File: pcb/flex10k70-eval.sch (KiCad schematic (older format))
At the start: 68 parts, among them CN1 IO_1, CN2 IO_2, CN3 IO_3, CN4 IO_4, CN5 FLASH, CN6 JTAG, SW1 SW_DIP_x04, SW2 SW_DIP_x04, U1 25LC1024-I/SM, U2 EPF10K70RC240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

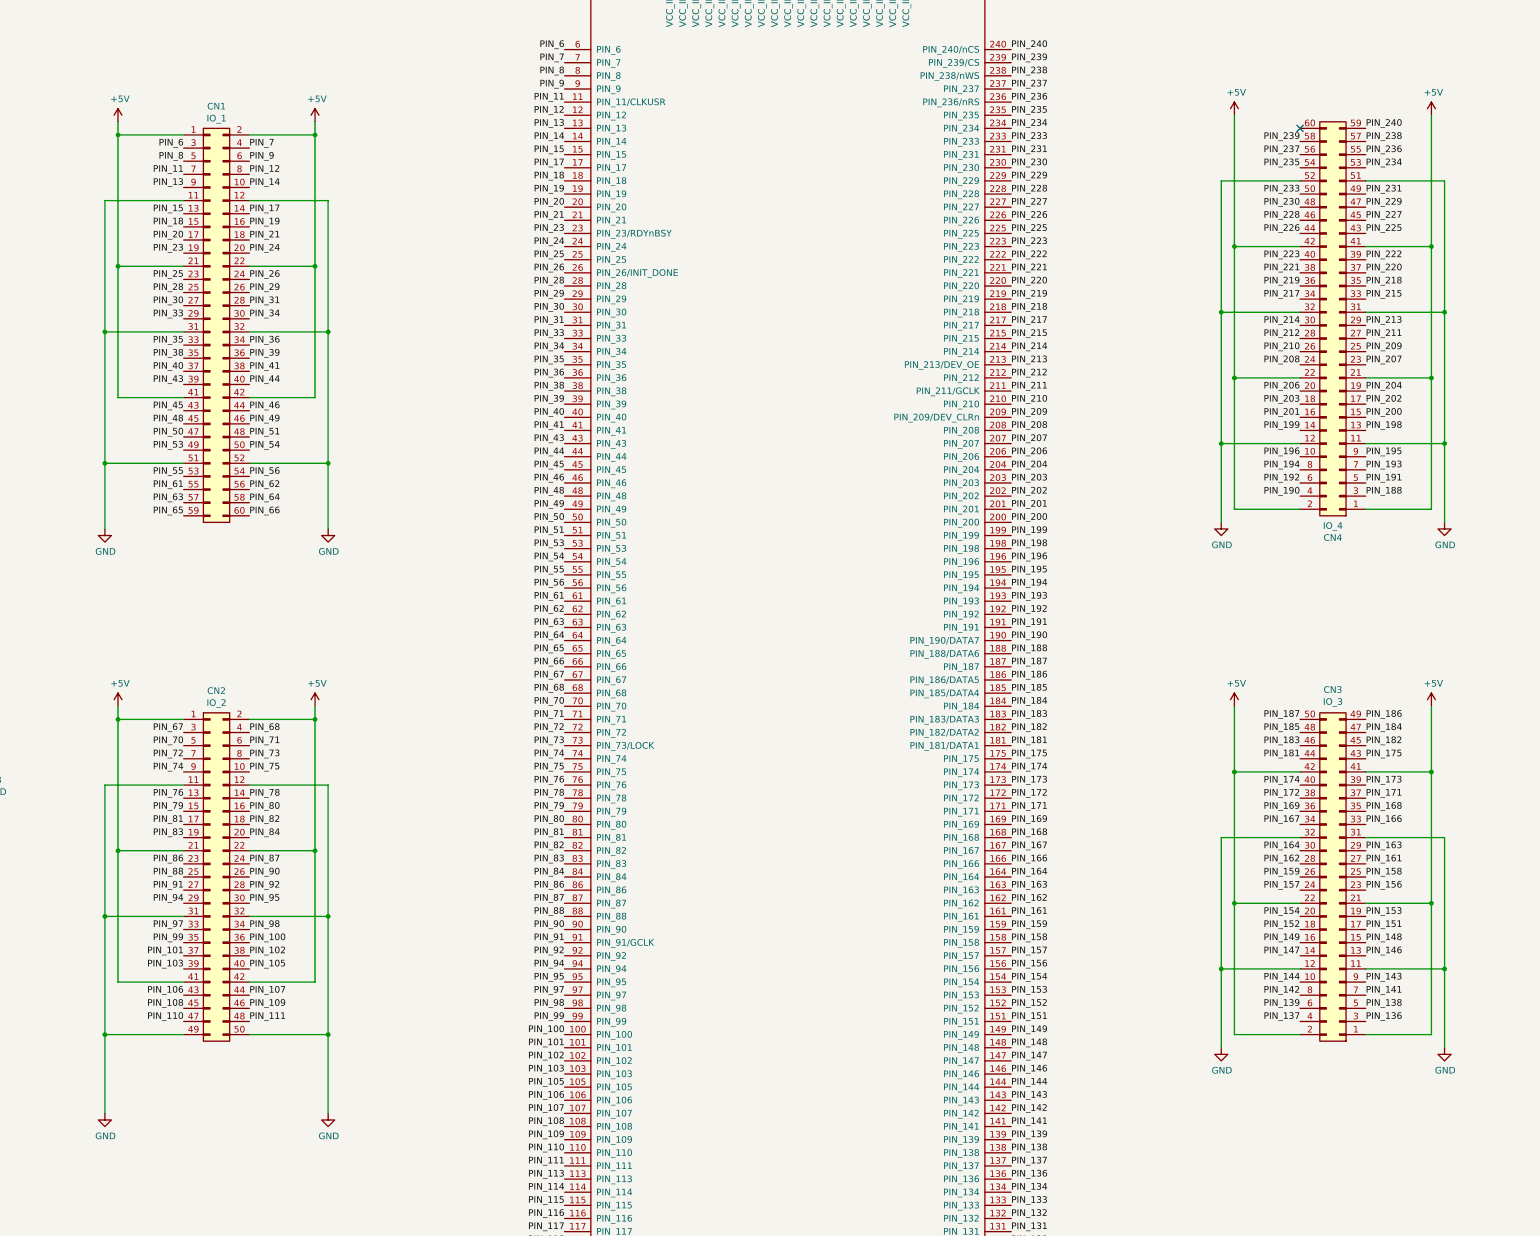
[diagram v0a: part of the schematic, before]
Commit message: modify CN3 CN4 pin orientation
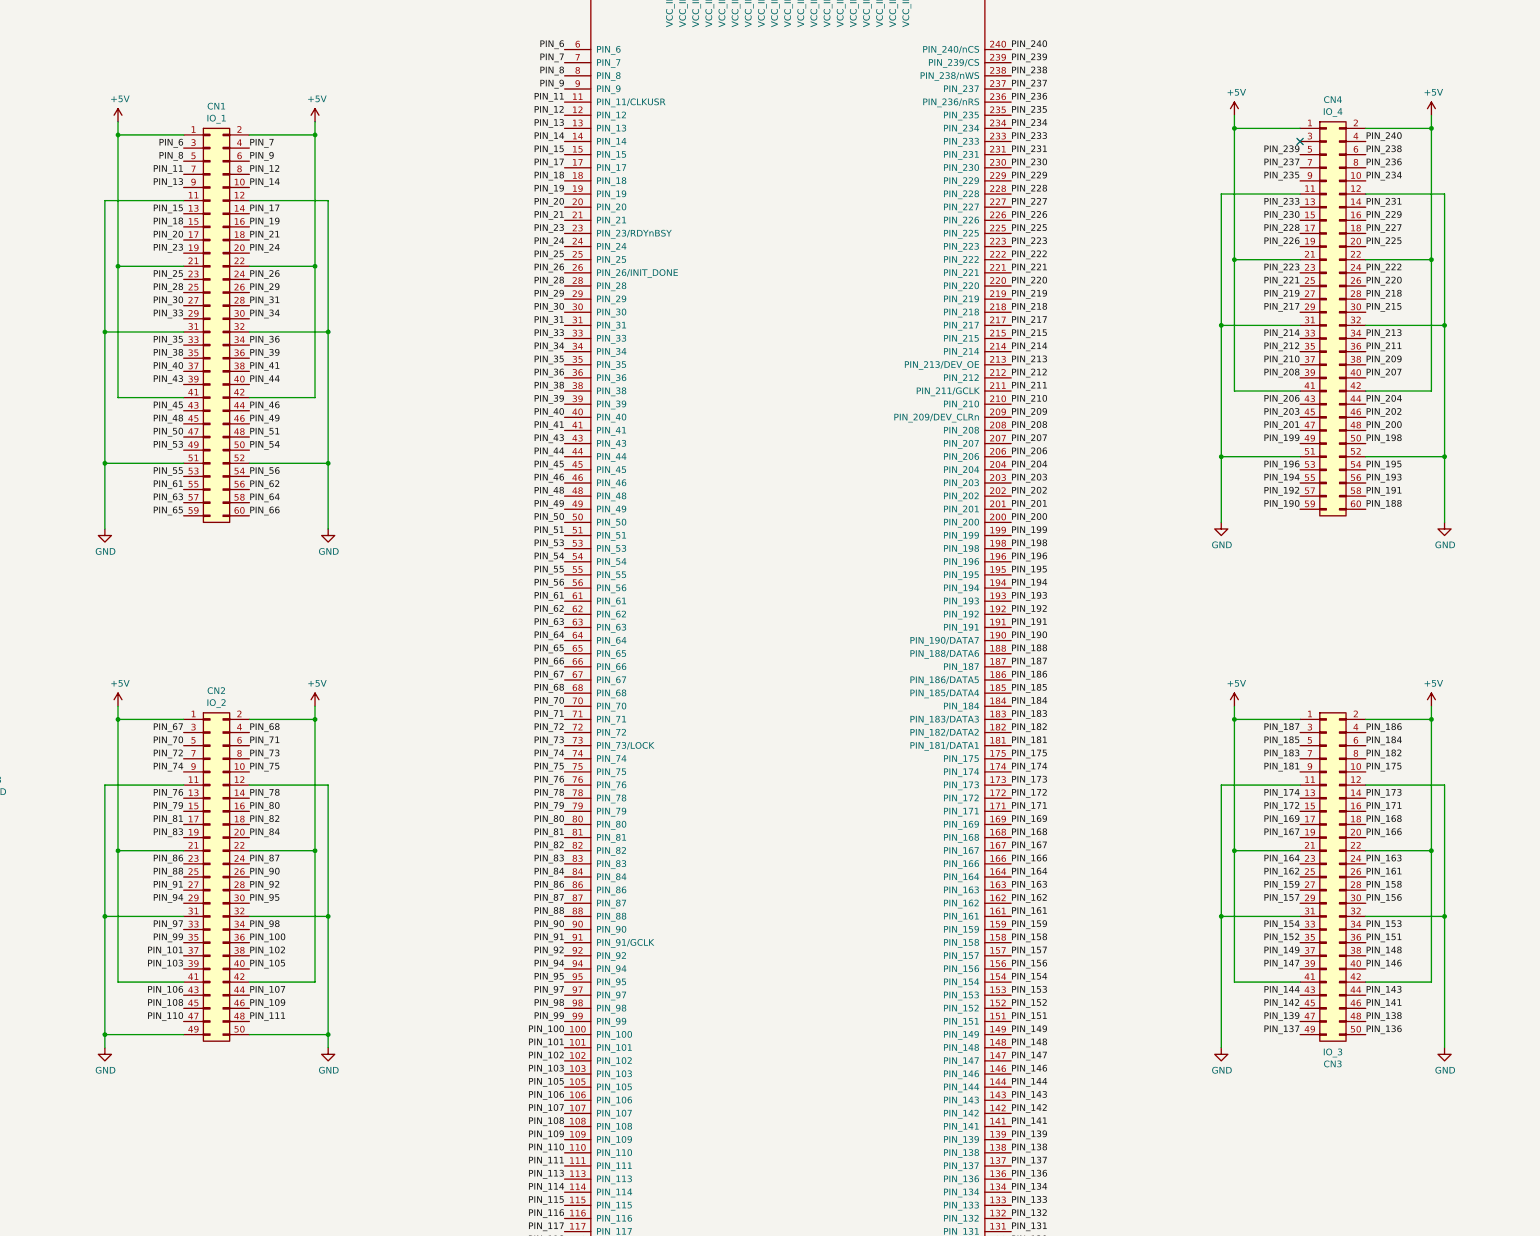
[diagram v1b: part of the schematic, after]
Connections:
- net PIN_136: now also CN3.50 (Pin_50); no longer CN3.3 (Pin_3)
- net PIN_137: now also CN3.49 (Pin_49); no longer CN3.4 (Pin_4)
- net PIN_138: now also CN3.48 (Pin_48); no longer CN3.5 (Pin_5)
- net PIN_139: now also CN3.47 (Pin_47); no longer CN3.6 (Pin_6)
- net PIN_141: now also CN3.46 (Pin_46); no longer CN3.7 (Pin_7)
- net PIN_142: now also CN3.45 (Pin_45); no longer CN3.8 (Pin_8)
- net PIN_143: now also CN3.44 (Pin_44); no longer CN3.9 (Pin_9)
- net PIN_144: now also CN3.43 (Pin_43); no longer CN3.10 (Pin_10)
- net PIN_146: now also CN3.40 (Pin_40); no longer CN3.13 (Pin_13)
- net PIN_147: now also CN3.39 (Pin_39); no longer CN3.14 (Pin_14)
- net PIN_148: now also CN3.38 (Pin_38); no longer CN3.15 (Pin_15)
- net PIN_149: now also CN3.37 (Pin_37); no longer CN3.16 (Pin_16)
- net PIN_151: now also CN3.36 (Pin_36); no longer CN3.17 (Pin_17)
- net PIN_152: now also CN3.35 (Pin_35); no longer CN3.18 (Pin_18)
- net PIN_153: now also CN3.34 (Pin_34); no longer CN3.19 (Pin_19)
- net PIN_154: now also CN3.33 (Pin_33); no longer CN3.20 (Pin_20)
- net PIN_156: now also CN3.30 (Pin_30); no longer CN3.23 (Pin_23)
- net PIN_157: now also CN3.29 (Pin_29); no longer CN3.24 (Pin_24)
- net PIN_158: now also CN3.28 (Pin_28); no longer CN3.25 (Pin_25)
- net PIN_159: now also CN3.27 (Pin_27); no longer CN3.26 (Pin_26)
- net PIN_161: now also CN3.26 (Pin_26); no longer CN3.27 (Pin_27)
- net PIN_162: now also CN3.25 (Pin_25); no longer CN3.28 (Pin_28)
- net PIN_163: now also CN3.24 (Pin_24); no longer CN3.29 (Pin_29)
- net PIN_164: now also CN3.23 (Pin_23); no longer CN3.30 (Pin_30)
- net PIN_166: now also CN3.20 (Pin_20); no longer CN3.33 (Pin_33)
- net PIN_167: now also CN3.19 (Pin_19); no longer CN3.34 (Pin_34)
- net PIN_168: now also CN3.18 (Pin_18); no longer CN3.35 (Pin_35)
- net PIN_169: now also CN3.17 (Pin_17); no longer CN3.36 (Pin_36)
- net PIN_171: now also CN3.16 (Pin_16); no longer CN3.37 (Pin_37)
- net PIN_172: now also CN3.15 (Pin_15); no longer CN3.38 (Pin_38)
- net PIN_173: now also CN3.14 (Pin_14); no longer CN3.39 (Pin_39)
- net PIN_174: now also CN3.13 (Pin_13); no longer CN3.40 (Pin_40)
- net PIN_175: now also CN3.10 (Pin_10); no longer CN3.43 (Pin_43)
- net PIN_181: now also CN3.9 (Pin_9); no longer CN3.44 (Pin_44)
- net PIN_182: now also CN3.8 (Pin_8); no longer CN3.45 (Pin_45)
- net PIN_183: now also CN3.7 (Pin_7); no longer CN3.46 (Pin_46)
- net PIN_184: now also CN3.6 (Pin_6); no longer CN3.47 (Pin_47)
- net PIN_185: now also CN3.5 (Pin_5); no longer CN3.48 (Pin_48)
- net PIN_186: now also CN3.4 (Pin_4); no longer CN3.49 (Pin_49)
- net PIN_187: now also CN3.3 (Pin_3); no longer CN3.50 (Pin_50)
- net PIN_188: now also CN4.60 (Pin_60); no longer CN4.3 (Pin_3)
- net PIN_190: now also CN4.59 (Pin_59); no longer CN4.4 (Pin_4)
- net PIN_191: now also CN4.58 (Pin_58); no longer CN4.5 (Pin_5)
- net PIN_192: now also CN4.57 (Pin_57); no longer CN4.6 (Pin_6)
- net PIN_193: now also CN4.56 (Pin_56); no longer CN4.7 (Pin_7)
- net PIN_194: now also CN4.55 (Pin_55); no longer CN4.8 (Pin_8)
- net PIN_195: now also CN4.54 (Pin_54); no longer CN4.9 (Pin_9)
- net PIN_196: now also CN4.53 (Pin_53); no longer CN4.10 (Pin_10)
- net PIN_198: now also CN4.50 (Pin_50); no longer CN4.13 (Pin_13)
- net PIN_199: now also CN4.49 (Pin_49); no longer CN4.14 (Pin_14)
- net PIN_200: now also CN4.48 (Pin_48); no longer CN4.15 (Pin_15)
- net PIN_201: now also CN4.47 (Pin_47); no longer CN4.16 (Pin_16)
- net PIN_202: now also CN4.46 (Pin_46); no longer CN4.17 (Pin_17)
- net PIN_203: now also CN4.45 (Pin_45); no longer CN4.18 (Pin_18)
- net PIN_204: now also CN4.44 (Pin_44); no longer CN4.19 (Pin_19)
- net PIN_206: now also CN4.43 (Pin_43); no longer CN4.20 (Pin_20)
- net PIN_207: now also CN4.40 (Pin_40); no longer CN4.23 (Pin_23)
- net PIN_208: now also CN4.39 (Pin_39); no longer CN4.24 (Pin_24)
- net PIN_209: now also CN4.38 (Pin_38); no longer CN4.25 (Pin_25)
- net PIN_210: now also CN4.37 (Pin_37); no longer CN4.26 (Pin_26)
- net PIN_211: now also CN4.36 (Pin_36); no longer CN4.27 (Pin_27)
- net PIN_212: now also CN4.35 (Pin_35); no longer CN4.28 (Pin_28)
- net PIN_213: now also CN4.34 (Pin_34); no longer CN4.29 (Pin_29)
- net PIN_214: now also CN4.33 (Pin_33); no longer CN4.30 (Pin_30)
- net PIN_215: now also CN4.30 (Pin_30); no longer CN4.33 (Pin_33)
- net PIN_217: now also CN4.29 (Pin_29); no longer CN4.34 (Pin_34)
- net PIN_218: now also CN4.28 (Pin_28); no longer CN4.35 (Pin_35)
- net PIN_219: now also CN4.27 (Pin_27); no longer CN4.36 (Pin_36)
- net PIN_220: now also CN4.26 (Pin_26); no longer CN4.37 (Pin_37)
- net PIN_221: now also CN4.25 (Pin_25); no longer CN4.38 (Pin_38)
- net PIN_222: now also CN4.24 (Pin_24); no longer CN4.39 (Pin_39)
- net PIN_223: now also CN4.23 (Pin_23); no longer CN4.40 (Pin_40)
- net PIN_225: now also CN4.20 (Pin_20); no longer CN4.43 (Pin_43)
- net PIN_226: now also CN4.19 (Pin_19); no longer CN4.44 (Pin_44)
- net PIN_227: now also CN4.18 (Pin_18); no longer CN4.45 (Pin_45)
- net PIN_228: now also CN4.17 (Pin_17); no longer CN4.46 (Pin_46)
- net PIN_229: now also CN4.16 (Pin_16); no longer CN4.47 (Pin_47)
- net PIN_230: now also CN4.15 (Pin_15); no longer CN4.48 (Pin_48)
- net PIN_231: now also CN4.14 (Pin_14); no longer CN4.49 (Pin_49)
- net PIN_233: now also CN4.13 (Pin_13); no longer CN4.50 (Pin_50)
- net PIN_234: now also CN4.10 (Pin_10); no longer CN4.53 (Pin_53)
- net PIN_235: now also CN4.9 (Pin_9); no longer CN4.54 (Pin_54)
- net PIN_236: now also CN4.8 (Pin_8); no longer CN4.55 (Pin_55)
- net PIN_237: now also CN4.7 (Pin_7); no longer CN4.56 (Pin_56)
- net PIN_238: now also CN4.6 (Pin_6); no longer CN4.57 (Pin_57)
- net PIN_239: now also CN4.5 (Pin_5); no longer CN4.58 (Pin_58)
- net PIN_240: now also CN4.4 (Pin_4); no longer CN4.59 (Pin_59)
